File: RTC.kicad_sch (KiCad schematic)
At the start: 14 parts, among them J17 Molex 470531000, U11 EMC2301-1-ACZL-TR, U14 74LVC1G07SE-7, U8 PCF85063AT/AAZ, Y2 X32K768S301

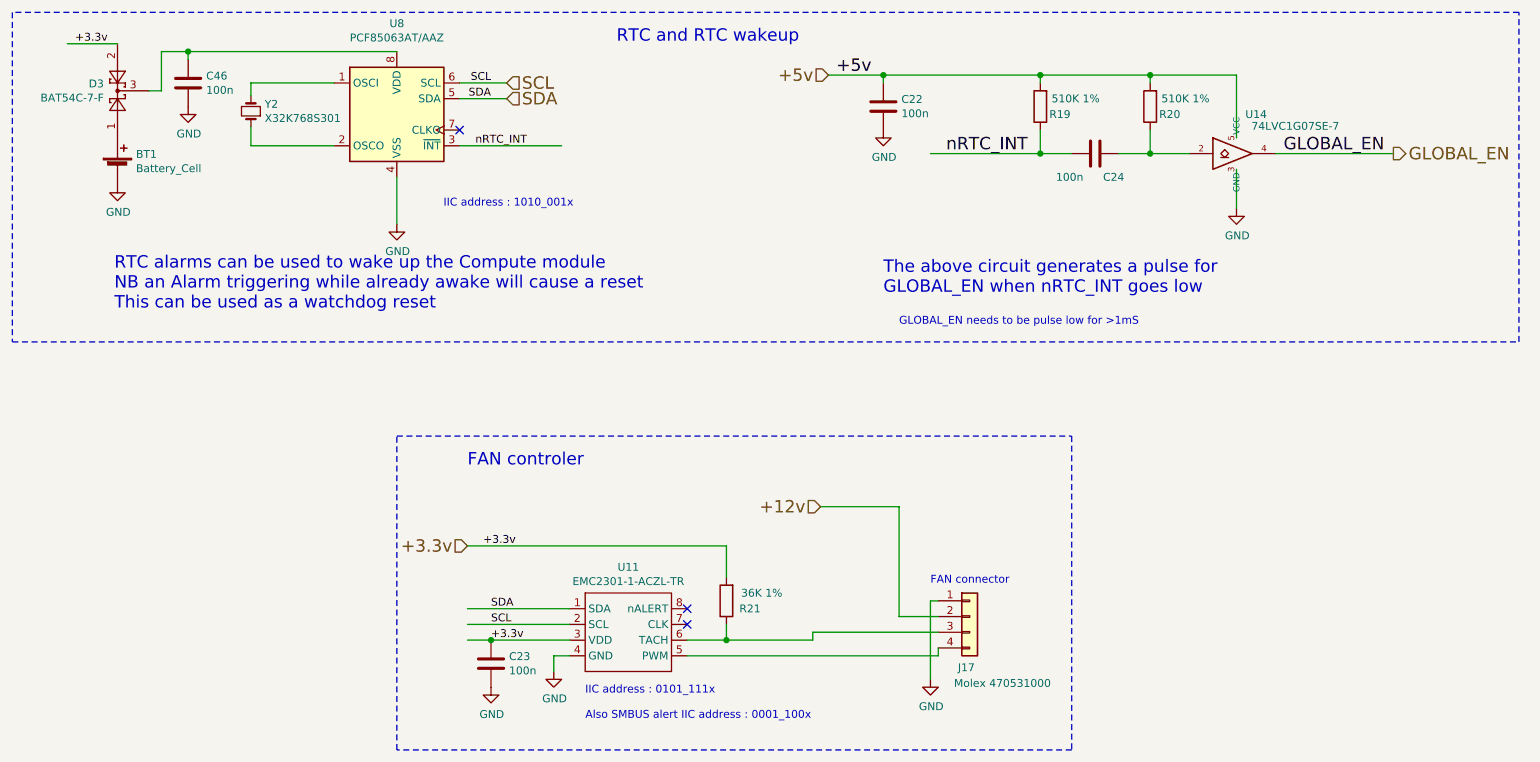
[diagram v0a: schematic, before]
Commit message: removed many unused parts
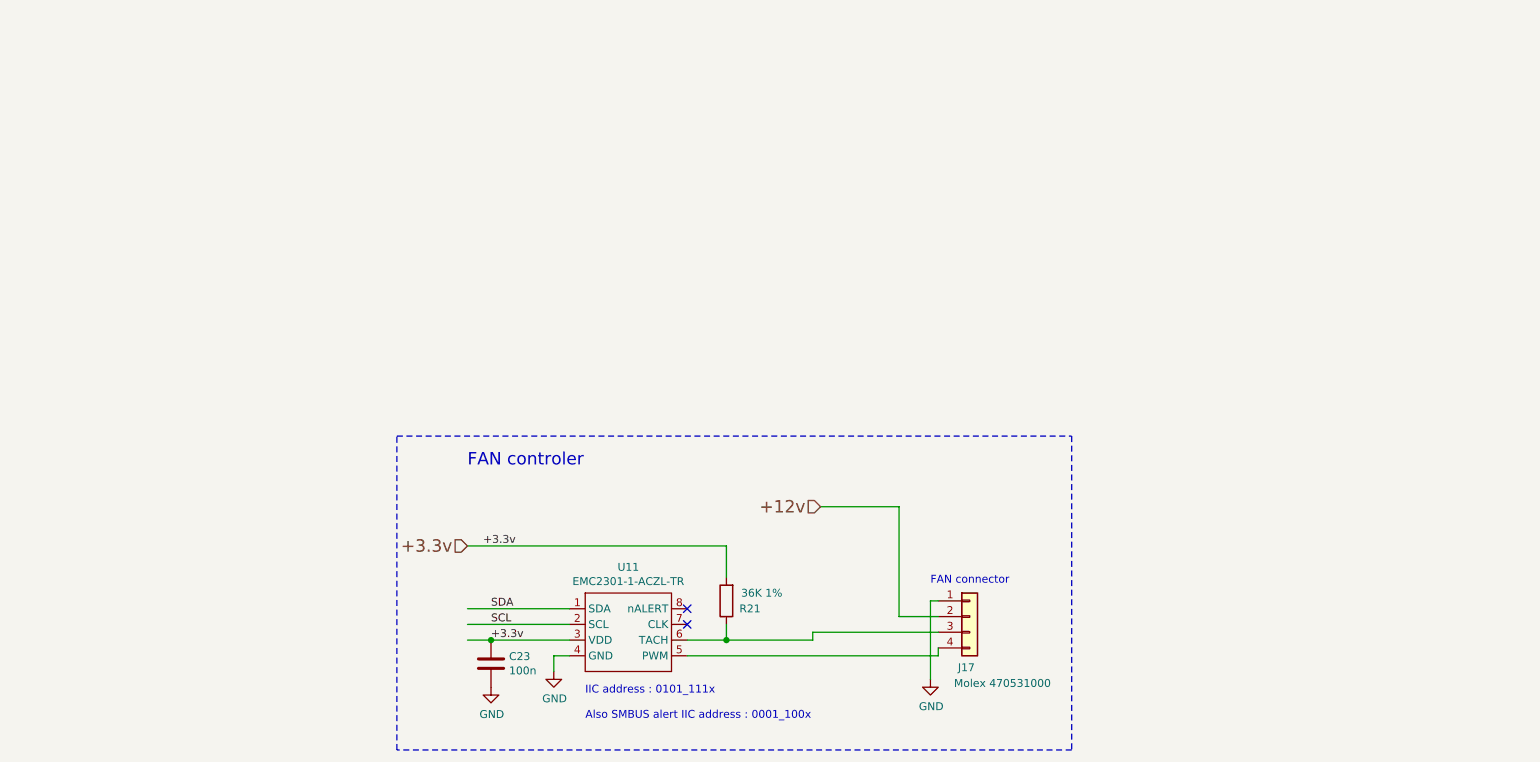
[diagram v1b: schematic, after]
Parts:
- removed BT1: Battery_Cell, Battery:BatteryHolder_Keystone_3034_1x20mm, symbol Device:Battery_Cell
- removed C22, C24, C46: 100n, Capacitor_SMD:C_0402_1005Metric, symbol Device:C
- removed D3: BAT54C-7-F, Package_TO_SOT_SMD:SOT-23, symbol Diode:BAT54C
- removed R19, R20: 510K 1%, Resistor_SMD:R_0402_1005Metric, symbol Device:R
- removed U14: 74LVC1G07SE-7, Package_TO_SOT_SMD:SOT-353_SC-70-5, symbol CM4IO:74LVC1G07_copy
- removed U8: PCF85063AT/AAZ, Package_SO:SOIC-8_3.9x4.9mm_P1.27mm, symbol Timer_RTC:PCF8563T
- removed Y2: X32K768S301, Crystal:Crystal_SMD_3215-2Pin_3.2x1.5mm, symbol Device:Crystal_Small
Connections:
- no-connect marks 3 -> 2
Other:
- note removed: "GLOBAL_EN needs to be pulse low for >1mS"
- note removed: "IIC address : 1010_001x"
- note removed: "RTC alarms can be used to wake up the Compute module NB an Alarm triggering while already awake will cause a reset This can be used as a watchdog reset"
- note removed: "RTC and RTC wakeup"
- note removed: "The above circuit generates a pulse for GLOBAL_EN when nRTC_INT goes low"
- company: © 2020-2022 Raspberry Pi Ltd (formerly Raspberry Pi (Trading) Ltd.) -> (none)

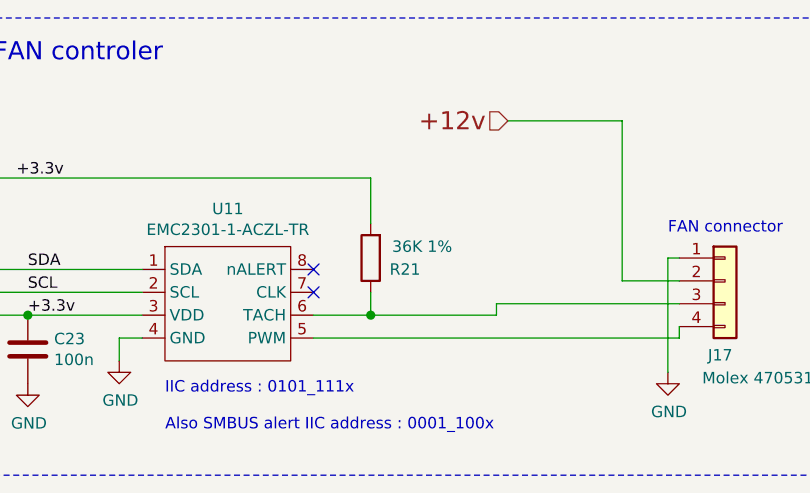
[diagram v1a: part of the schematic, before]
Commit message: changed PoE transformer to Wurth 7491194912
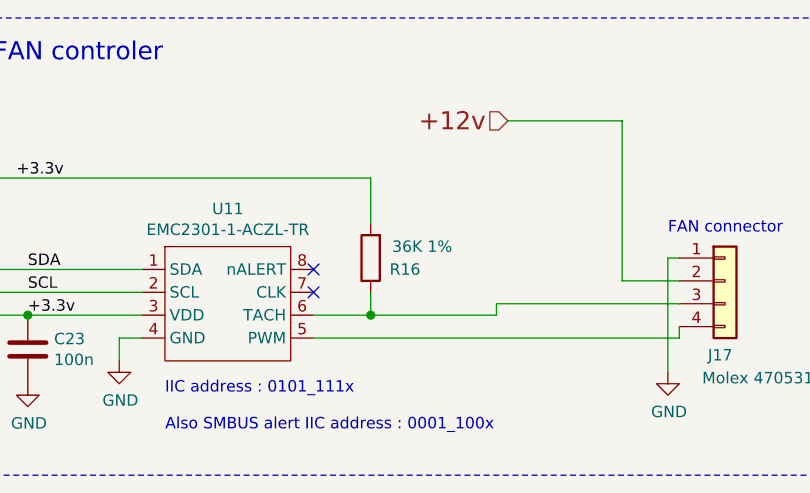
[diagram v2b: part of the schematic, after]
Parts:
- renumbered R21 to R16
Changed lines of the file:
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@@
   (symbol (lib_id "Device:R") (at 144.78 134.62 180) (unit 1)
     (in_bom yes) (on_board yes)
-    (property "Reference" "R21" (id 0) (at 148.59 135.89 0))
+    (property "Reference" "R16" (id 0) (at 148.59 135.89 0))
     (property "Value" "36K 1%" (id 1) (at 150.495 133.35 0))
     (property "Footprint" "Resistor_SMD:R_0402_1005Metric" (id 2) (at 146.558 134.62 90)

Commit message: started routing PoE
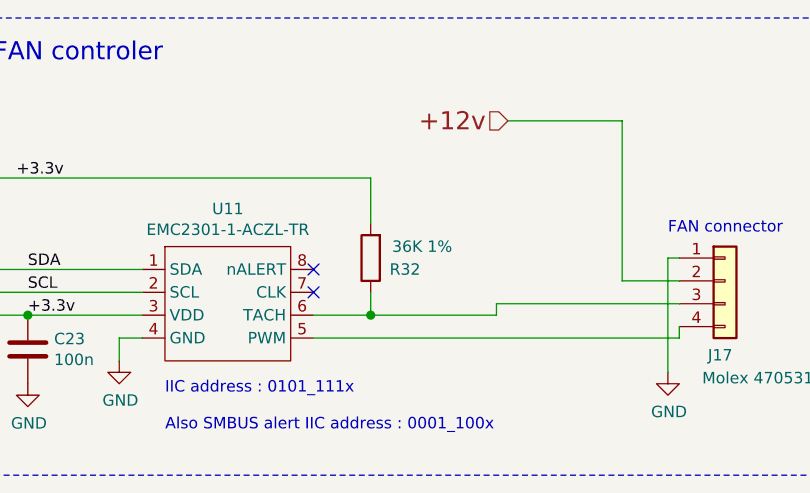
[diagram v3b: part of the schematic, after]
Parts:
- renumbered R16 to R32
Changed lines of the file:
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@@
   (symbol (lib_id "Device:R") (at 144.78 134.62 180) (unit 1)
     (in_bom yes) (on_board yes)
-    (property "Reference" "R16" (id 0) (at 148.59 135.89 0))
+    (property "Reference" "R32" (id 0) (at 148.59 135.89 0))
     (property "Value" "36K 1%" (id 1) (at 150.495 133.35 0))
     (property "Footprint" "Resistor_SMD:R_0402_1005Metric" (id 2) (at 146.558 134.62 90)
